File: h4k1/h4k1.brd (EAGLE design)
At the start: 250 x 80 mm, 186 parts, among them IC1 STM32F10XCXT6, J2 PJ-313D-AUDIO-JACK, J3 USB-AF10, K1 CHERRY-MX-LED, K10 CHERRY-MX, K11 CHERRY-MX, K12 CHERRY-MX, K13 CHERRY-MX, K14 CHERRY-MX, K15 CHERRY-MX, K16 CHERRY-MX, K17 CHERRY-MX-LED, K18 CHERRY-MX, K19 CHERRY-MX, K2 CHERRY-MX-LED, K20 CHERRY-MX, K21 CHERRY-MX, K22 CHERRY-MX, K23 CHERRY-MX, K24 CHERRY-MX, K25 CHERRY-MX-LED, K26 CHERRY-MX, K27 CHERRY-MX, K28 CHERRY-MX, K29 CHERRY-MX, K3 CHERRY-MX-LED, K30 CHERRY-MX, K31 CHERRY-MX, K32 CHERRY-MX, K33 CHERRY-MX-LED, K34 CHERRY-MX, K35 CHERRY-MX, K36 CHERRY-MX-LED, K37 CHERRY-MX-LED, K38 CHERRY-MX, K39 CHERRY-MX, K4 CHERRY-MX-LED, K40 CHERRY-MX-LED, K41 CHERRY-MX, K42 CHERRY-MX, K43 CHERRY-MX, K44 CHERRY-MX, K45 CHERRY-MX, K46 CHERRY-MX-LED, K5 CHERRY-MX-LED, K6 CHERRY-MX-LED, K65 EVQPUL02K, K66 EVQPUL02K, K67 K3-1280S-F2, K7 CHERRY-MX-LED, K8 CHERRY-MX-LED, K9 CHERRY-MX-LED, U1 G850G, U3 PCM2704CDB, X4 12M

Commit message: WIP: led layout
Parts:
- added R39, R40, R41, R42: 200, hqc:0805
- added T1: DBG, hqc-connector:CLIP-8P-1.27
- moved C32 0.71 mm to (25.9, 35.7)
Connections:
- removed net SWDCLK: IC1.37
- new net LED_C1: IC1.21, K1.LED_P, K17.LED_P, K25.LED_P, K9.LED_P
- new net LED_C2: IC1.22, K2.LED_P, K3.LED_P, K5.LED_P, K6.LED_P
- new net LED_C3: IC1.25, K4.LED_P, K40.LED_P, K7.LED_P, K8.LED_P
- new net LED_C4: IC1.26, K33.LED_P, K36.LED_P, K37.LED_P, K46.LED_P
- new net LED_R1: K25.LED_N, K46.LED_N, K6.LED_N, K7.LED_N, R39.P$2
- new net LED_R2: K17.LED_N, K33.LED_N, K5.LED_N, K8.LED_N, R40.P$2
- new net LED_R3: K3.LED_N, K37.LED_N, K4.LED_N, K9.LED_N, R41.P$2
- new net LED_R4: K1.LED_N, K2.LED_N, K36.LED_N, K40.LED_N, R42.P$2
- new net N$76: IC1.29, R39.P$1
- new net N$80: IC1.30, R40.P$1
- new net N$81: IC1.31, R41.P$1
- new net N$85: IC1.38, R42.P$1
- new net SWCLK: IC1.37, T1.P$7
- net GND: now also T1.P$8
- net SWDIO: now also T1.P$6
- net VDD: now also T1.P$5
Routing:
- net LED_R4: track 0.00 -> 273.5 mm, vias 0 -> 2
- net LED_R2: track 0.00 -> 146.5 mm, vias 0 -> 3
- net N$80: track 0.00 -> 145.8 mm, vias 0 -> 2
- net N$85: track 0.00 -> 134.4 mm, vias 0 -> 4
- net LED_C1: track 0.00 -> 82.5 mm, vias 0 -> 1
- net N$81: track 0.00 -> 78.9 mm, vias 0 -> 2
- net LED_C4: track 0.00 -> 65.3 mm, vias 0 -> 1
- net LED_R3: track 0.00 -> 59.1 mm, vias 0 -> 2
- net LED_C2: track 0.00 -> 47.4 mm, vias 0 -> 1
- net LED_C3: track 0.00 -> 32.5 mm, vias 0 -> 2
- net LED_R1: track 0.00 -> 27.2 mm
- net USB1+: track 185.1 -> 166.5 mm
- net USB1-: track 183.4 -> 167.4 mm
- net SWCLK: track 0.00 -> 7.63 mm, vias 0 -> 1
- net N$76: track 0.00 -> 7.47 mm, vias 0 -> 1
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
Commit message: update keyboard layout
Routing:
- net LED_R1: track 27.2 -> 367.2 mm
- net LED_R3: track 59.1 -> 307.7 mm, vias 2 -> 6
- net LED_C1: track 82.5 -> 252.4 mm, vias 1 -> 6
- net N$76: track 7.47 -> 163.4 mm, vias 1 -> 2
- net VDD: track 257.7 -> 338.6 mm, vias 7 -> 8
- net LED_C2: track 47.4 -> 126.6 mm, vias 1 -> 3
- net LED_R2: track 146.5 -> 225.5 mm
- net LED_C3: track 32.5 -> 84.3 mm
- net LED_C4: track 65.3 -> 89.9 mm, vias 1 -> 6
- net N$20: track 344.4 -> 328.5 mm, vias 9 -> 11
- net N$5: track 341.7 -> 340.3 mm
- net KB_R3: track 183.9 -> 184.9 mm
- net KB_R4: track 197.3 -> 198.1 mm
- net KB_C1: track 20.4 -> 19.9 mm
- net N$11: vias 13 -> 15

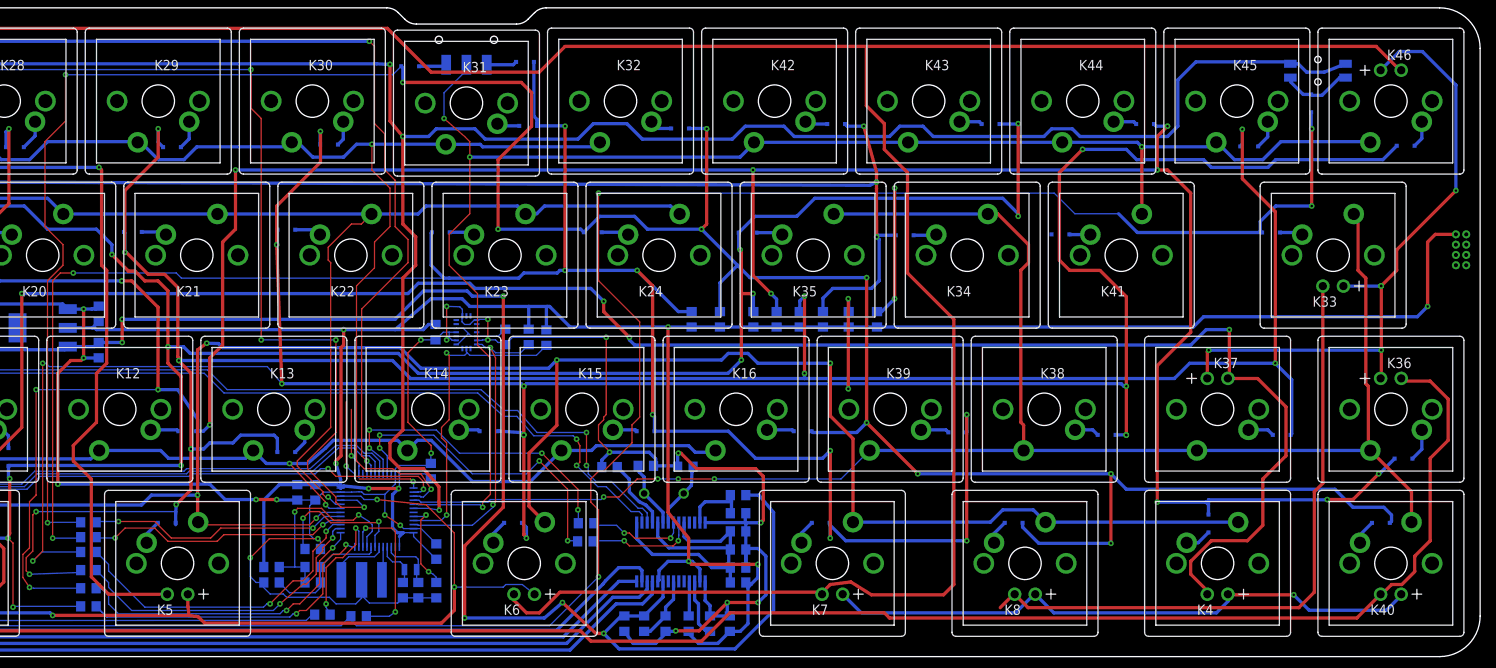
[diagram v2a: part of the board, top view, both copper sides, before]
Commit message: keyboard layout done not checked
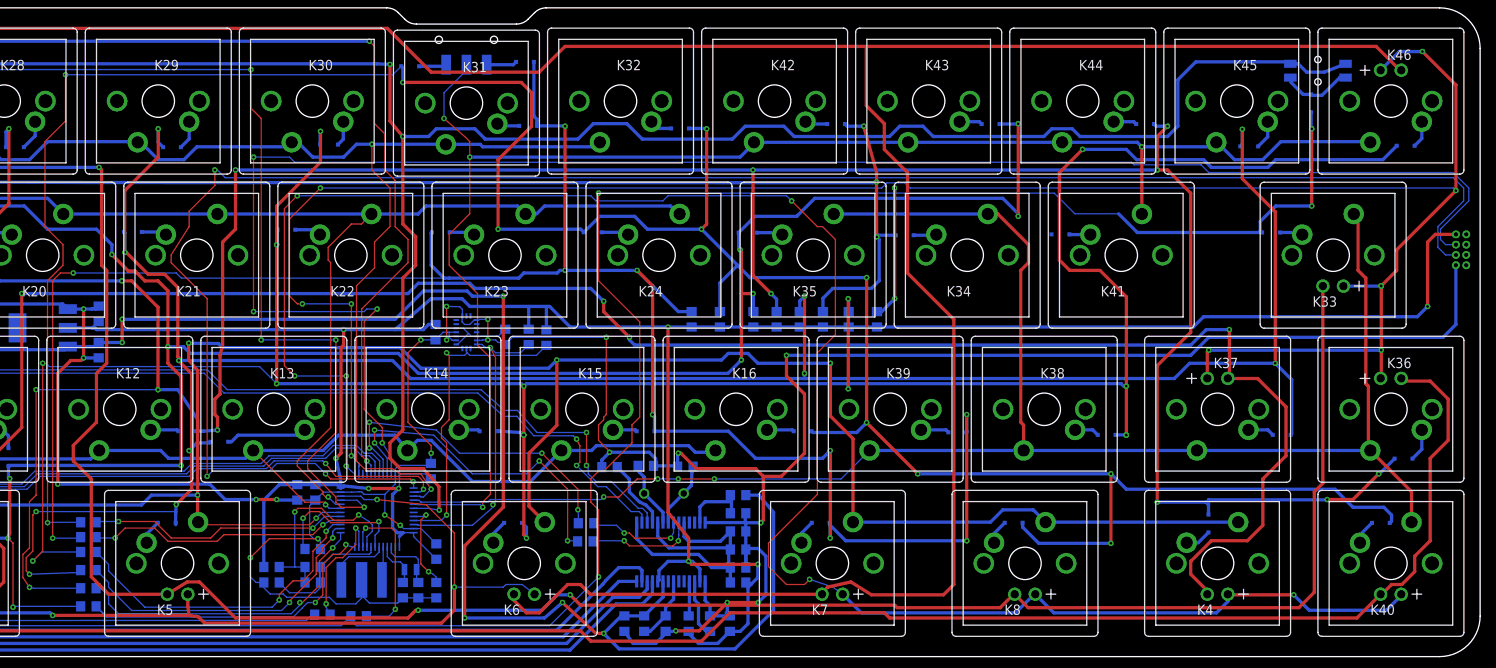
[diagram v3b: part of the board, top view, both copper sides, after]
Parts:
- moved D13 8.35 mm to (94.5, 26.5)
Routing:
- net SWCLK: track 7.63 -> 235.5 mm, vias 1 -> 4
- net SWDIO: track 0.00 -> 218.1 mm, vias 0 -> 4
- net LED_C4: track 89.9 -> 266.5 mm, vias 6 -> 10
- net LED_C3: track 84.3 -> 240.9 mm, vias 2 -> 7
- net GND: track 475.6 -> 586.3 mm, vias 31 -> 32
- net LED_R2: track 225.5 -> 332.4 mm, vias 3 -> 5
- net N$13: track 298.2 -> 288.5 mm
- net N$27: track 3.22 -> 10.0 mm
- net KB_R2: track 160.1 -> 163.8 mm, vias 2 -> 1
- net KB_R1: track 293.1 -> 295.1 mm
- net N$74: track 40.0 -> 41.5 mm
- net N$72: track 39.2 -> 40.3 mm
- net LED_R1: track 367.2 -> 368.2 mm
- net N$11: track 366.5 -> 367.5 mm
- net N$85: track 134.4 -> 135.3 mm

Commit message: resolve drc problem
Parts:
- C10, C11: value 4.7uF -> 28pF
- X3: value (none) -> 12MHz
- moved R39 85.8 mm to (97.1, 71.8), turned to 90 degrees
- moved D30 6.86 mm to (114.4, 65.6), turned to 0 degrees
- moved D5 3.21 mm to (85.5, 18.4), turned to 270 degrees
- moved R30 0.33 mm to (44.1, 34.6), turned to 180 degrees
- moved C22 0.15 mm to (50.7, 34.2)
- moved C26 0.15 mm to (37.5, 46.1)
- moved R27 0.15 mm to (52.8, 34.2)
- moved R28 0.15 mm to (48.8, 34.6)
- moved R29 0.15 mm to (46.9, 34.6)
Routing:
- net N$76: track 163.4 -> 78.6 mm, vias 2 -> 3
- net GND: track 586.3 -> 647.4 mm, vias 32 -> 31
- net LED_R2: track 332.4 -> 387.6 mm, vias 5 -> 6
- net N$2: track 371.7 -> 347.4 mm, vias 10 -> 12
- net KB_R6: track 191.9 -> 207.4 mm
- net N$80: track 145.9 -> 131.0 mm
- net KB_R5: track 213.2 -> 227.8 mm
- net N$17: track 246.1 -> 233.3 mm
- net KB_R7: track 294.0 -> 304.0 mm
- net LED_R4: track 273.5 -> 282.7 mm
- net N$13: track 288.5 -> 279.6 mm
- net USB2+: track 138.4 -> 129.7 mm, vias 2 -> 6
- net N$85: track 135.3 -> 127.3 mm, vias 4 -> 2
- net SWCLK: track 235.5 -> 228.9 mm
- net USB1+: track 166.5 -> 172.8 mm
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
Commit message: layout done
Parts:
- C20, C21: value (none) -> 28pF
- U1: value G850G -> GL850G
- X4: value 12M -> 12MHz

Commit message: add mounting holes
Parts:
- added U$1: COOBOC-PLACE, hqc-logo:COOBOC-PLACE
- added U$2, U$3, U$5, U$6, U$7, U$8: M2-MOUNTING-HOLE, hqc:M2-MOUNTING-HOLE
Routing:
- net N$2: track 347.4 -> 350.7 mm
- net LED_R2: track 387.6 -> 390.7 mm
- net LED_R4: track 282.7 -> 281.6 mm
- net N$20: track 330.5 -> 331.3 mm
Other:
- board text added: ">H4K-v0.1 20170731<"
